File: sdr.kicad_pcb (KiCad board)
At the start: 4 copper layers, 65 x 56 mm, 224 parts, among them J1 RX, J2 TX, SW1 KMR231NGLFS, T1 B0322J5050, T2 B0322J5050, T3 TR_TC1-1-43X+, T4 TR_TC1-1-43X+, U1 FT601, U10 MIC94310, U11 PAM2305, U12 BGS12, U13 BGS12, U14 FT232HL, U15 93LCxxBT-I/OT, U3 LMS6002DR2, U4 ECP5, U5 Si5351, U6 PAM2305, U7 LD39200, U8 MIC94310, U9 MIC94310, X1 GSB443133HR, X2 JTAG, X3 RaspberryPiConnector, X4 JTAG, X5 USB_OTG, Y1 FL3000027, Y2 ABM11-141, Y3 ABLS2-12.000MHZ-D4Y-T

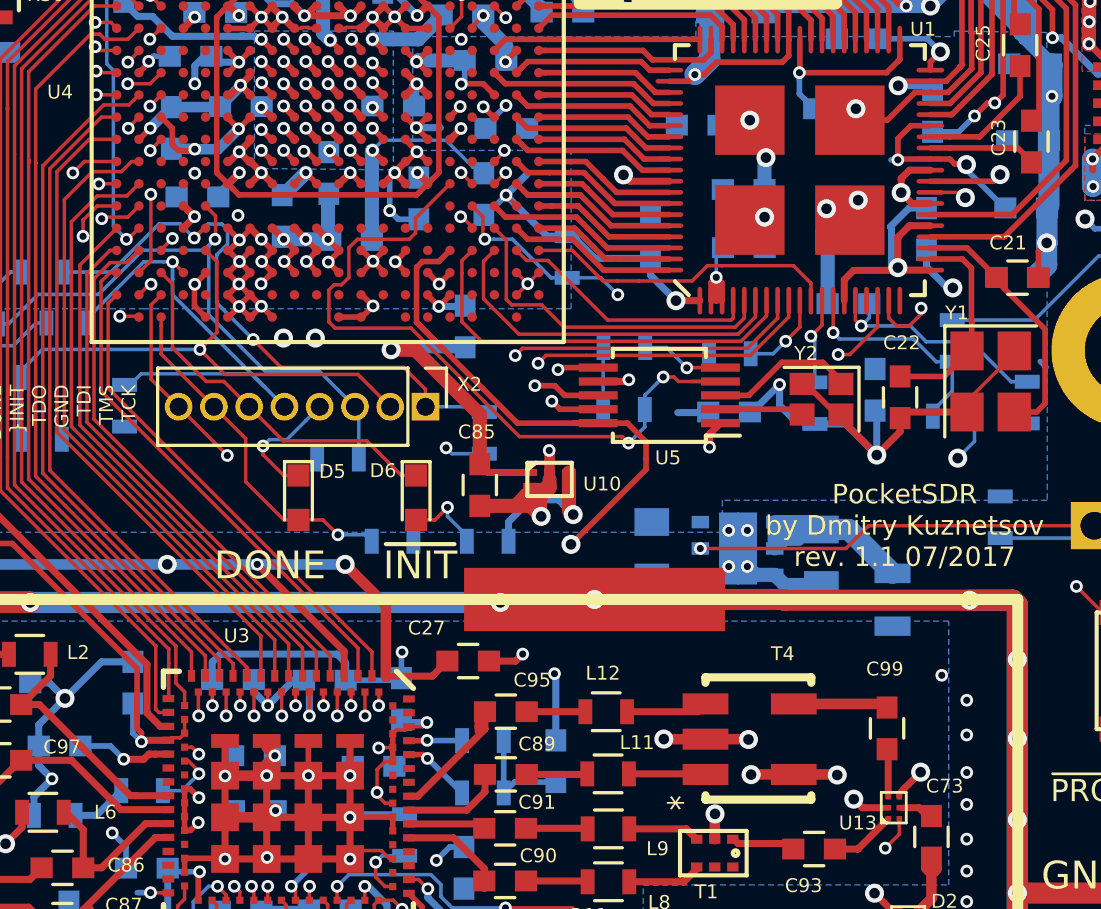
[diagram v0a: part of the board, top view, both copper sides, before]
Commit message: Update solder paste layer for components. Reduced width of tracks where they were wider than pads. Add mounting holes on paste layers.
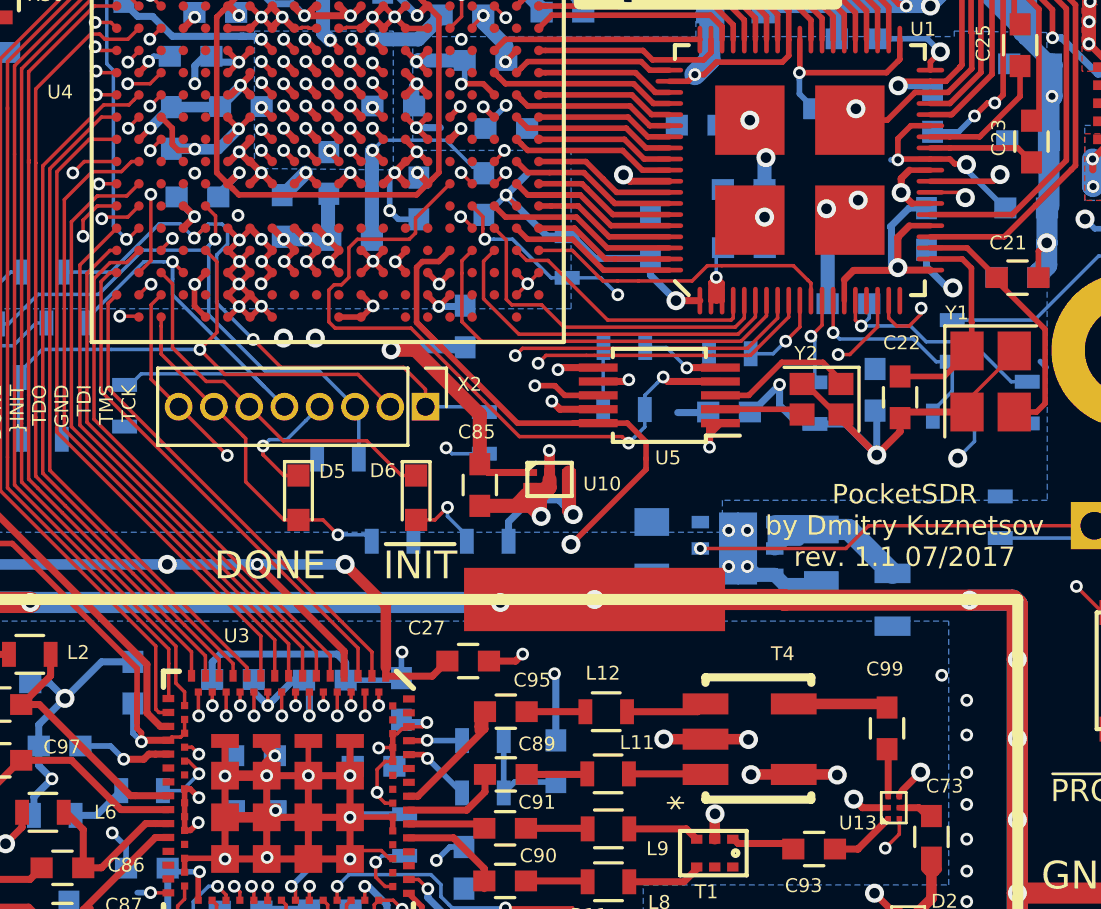
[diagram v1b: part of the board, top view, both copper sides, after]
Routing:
- net /FT601/I2C_SCL: track 26.7 -> 25.7 mm
- net VCCIO_FT: track 133.0 -> 133.7 mm

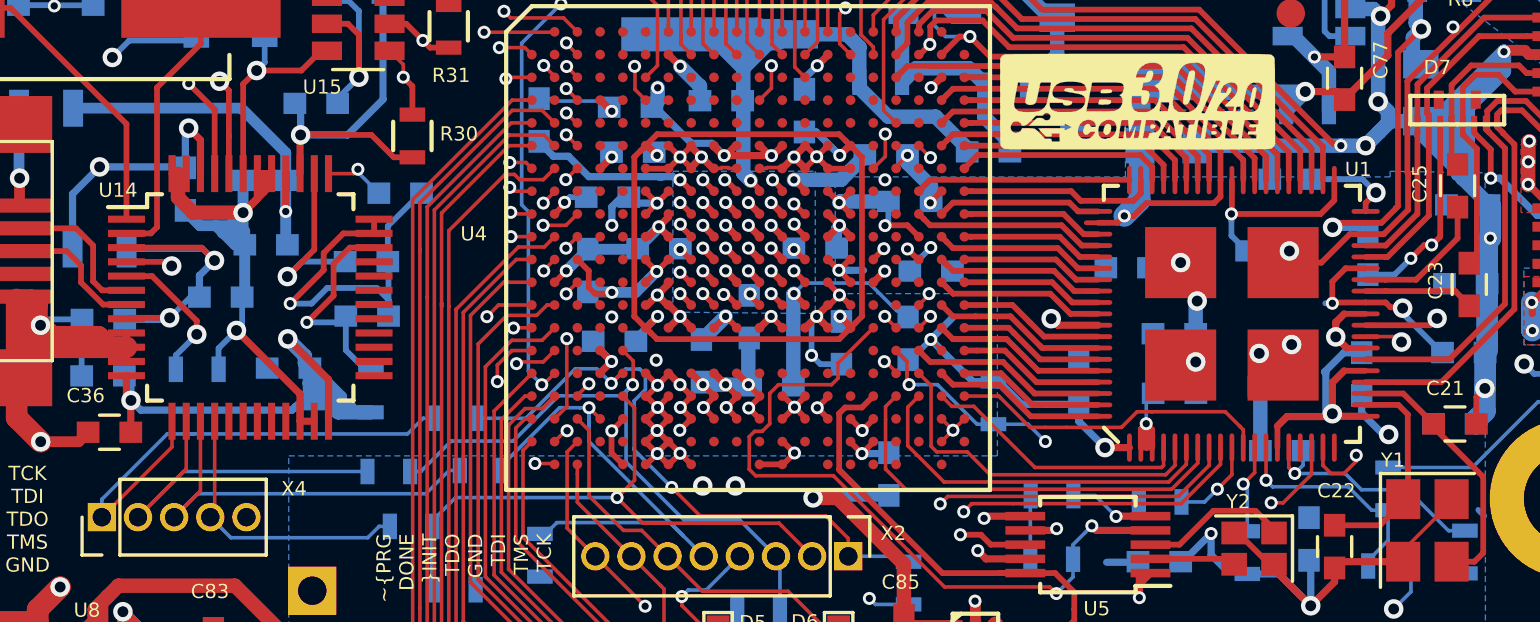
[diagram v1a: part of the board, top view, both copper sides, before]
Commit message: Update solder paste layers to reduce paste amount on some components and remove paste but not drill hole) on mount holes. Updated BOM. Removed deadend line on PCB. Add GND layer on Layer 3.
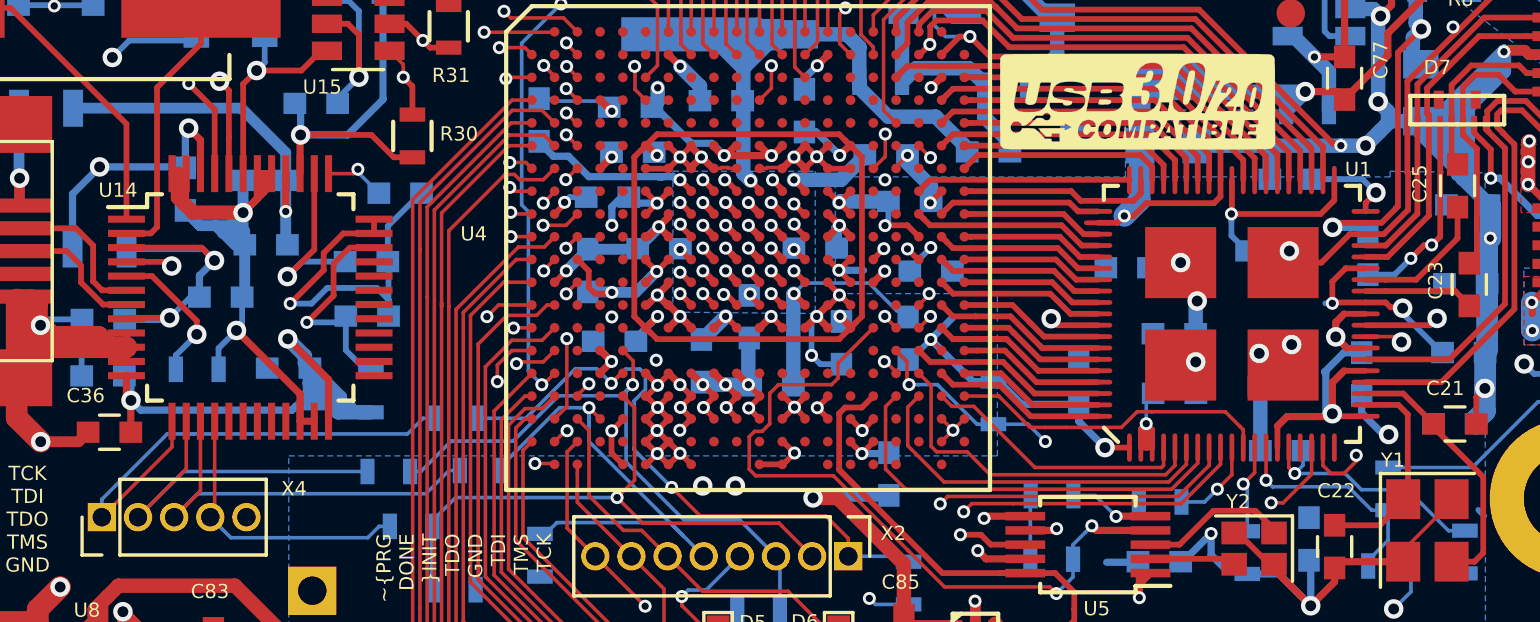
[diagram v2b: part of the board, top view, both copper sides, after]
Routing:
- net Net-(R39-Pad2): track 112.7 -> 49.4 mm
- net FT_GPIO1: track 72.3 -> 68.5 mm
- net GNDD: track 852.5 -> 853.6 mm
- added copper zone on In2.Cu, net GNDD

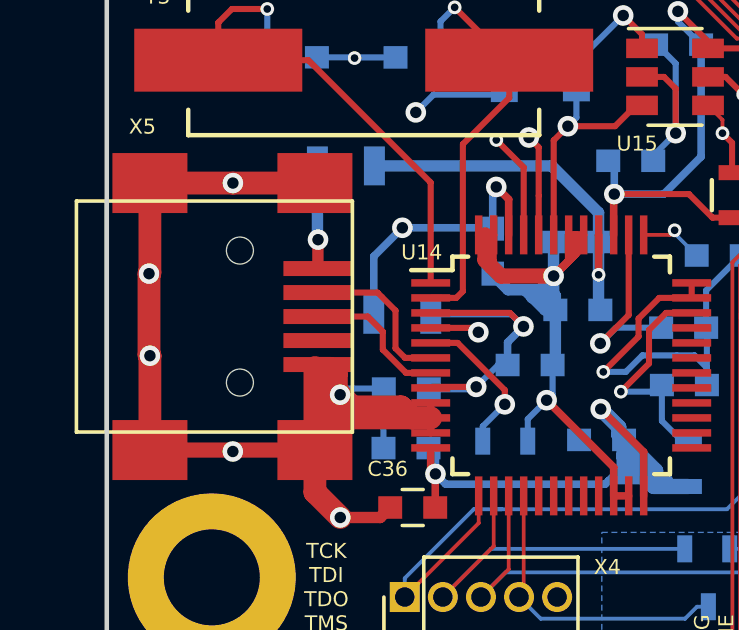
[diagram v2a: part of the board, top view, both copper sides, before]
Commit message: Fix USB mini B mount holes.
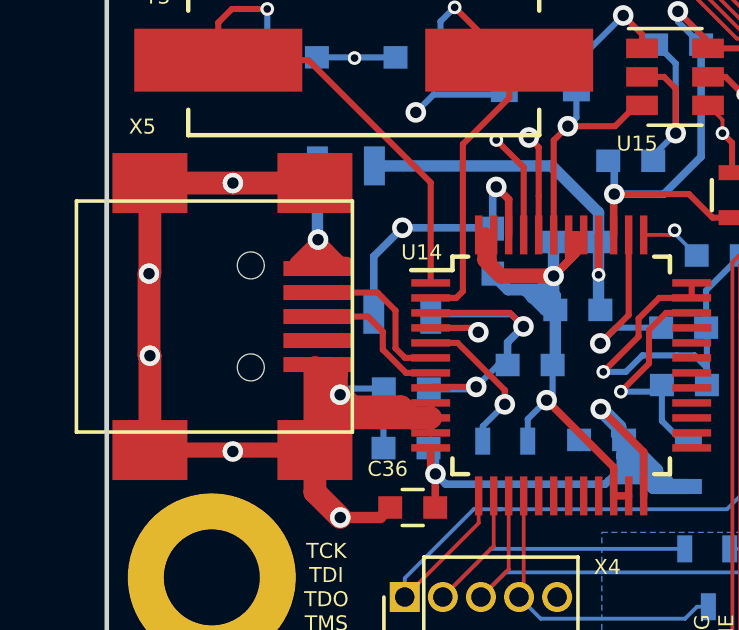
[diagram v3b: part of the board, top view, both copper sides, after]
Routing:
- net Net-(L13-Pad2): track 3.48 -> 7.55 mm
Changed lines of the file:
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@@
     (thickness 1.6)
     (drawings 27)
-    (tracks 3889)
+    (tracks 3897)
     (zones 0)
     (modules 224)
@@
     (0 F.Cu signal)
     (1 In1.Cu power hide)
-    (2 In2.Cu signal)
+    (2 In2.Cu signal hide)
     (31 B.Cu signal)
     (32 B.Adhes user hide)
@@
   )
   (setup
-    (last_trace_width 0.2032)
+    (last_trace_width 0.381)
     (user_trace_width 0.2032)
     (user_trace_width 0.254)
@@
     )
   )
-  (module Connectors:USB_Mini-B (layer F.Cu)
+  (module Connectors:USB_Mini-B locked (layer F.Cu)
     (at 104.23718 117.80556)
     (descr "USB Mini-B 5-pin SMD connector")
@@
     (pad 6 smd rect (at -2.8 4.45) (size 2.5 2) (layers F.Cu F.Paste F.Mask)
       (net 3 GNDD))
-    (pad "" np_thru_hole circle (at 0.2 -2.2) (size 0.9 0.9) (drill 0.9) (layers *.Cu *.Mask))
-    (pad "" np_thru_hole circle (at 0.2 2.2) (size 0.9 0.9) (drill 0.9) (layers *.Cu *.Mask))
+    (pad "" np_thru_hole circle (at 0.56282 -1.70556) (size 0.9 0.9) (drill 0.9) (layers *.Cu *.Mask))
+    (pad "" np_thru_hole circle (at 0.56282 1.69444) (size 0.9 0.9) (drill 0.9) (layers *.Cu *.Mask))
   )
   (module Inductors_SMD:L_0805 (layer B.Cu)
@@
   (segment (start 156.8577 133.25926) (end 159.80086 133.25926) (width 0.127) (layer B.Cu) (net 340))
   (segment (start 159.80086 133.25926) (end 160.24606 132.81406) (width 0.127) (layer B.Cu) (net 340))
+  (segment (start 106.875373 115.89258) (end 106.70286 115.89258) (width 0.381) (layer F.Cu) (net 341))
+  (segment (start 107.04068 115.24234) (end 107.04068 115.727273) (width 0.381) (layer F.Cu) (net 341))
+  (segment (start 107.04068 115.727273) (end 106.875373 115.89258) (width 0.381) (layer F.Cu) (net 341))
+  (segment (start 107.38612 115.58778) (end 107.38612 115.93576) (width 0.381) (layer F.Cu) (net 341))
+  (segment (start 107.04068 115.24234) (end 107.38612 115.58778) (width 0.381) (layer F.Cu) (net 341))
+  (segment (start 107.04068 115.24234) (end 106.28302 116) (width 0.381) (layer F.Cu) (net 341))
+  (segment (start 107.79834 116) (end 108 116) (width 0.381) (layer F.Cu) (net 341))
+  (segment (start 107.04068 115.24234) (end 107.79834 116) (width 0.381) (layer F.Cu) (net 341))
   (segment (start 107.02032 112.78362) (end 107.02032 115.22198) (width 0.381) (layer B.Cu) (net 341))
   (segment (start 107.02032 115.22198) (end 107.04068 115.24234) (width 0.381) (layer B.Cu) (net 341))

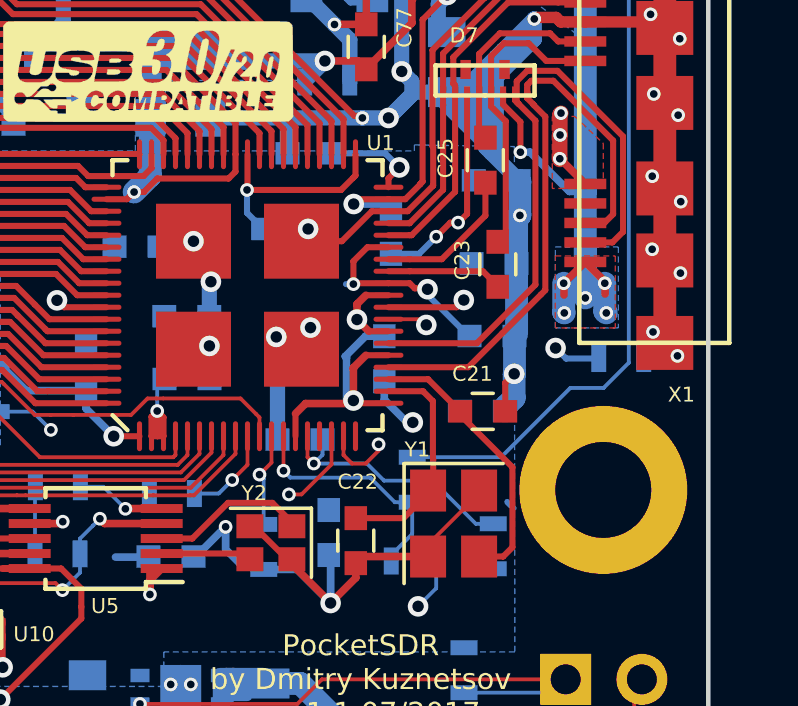
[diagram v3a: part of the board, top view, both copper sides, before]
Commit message: Small upgrade to make GND polygon on layer 3 more solid.
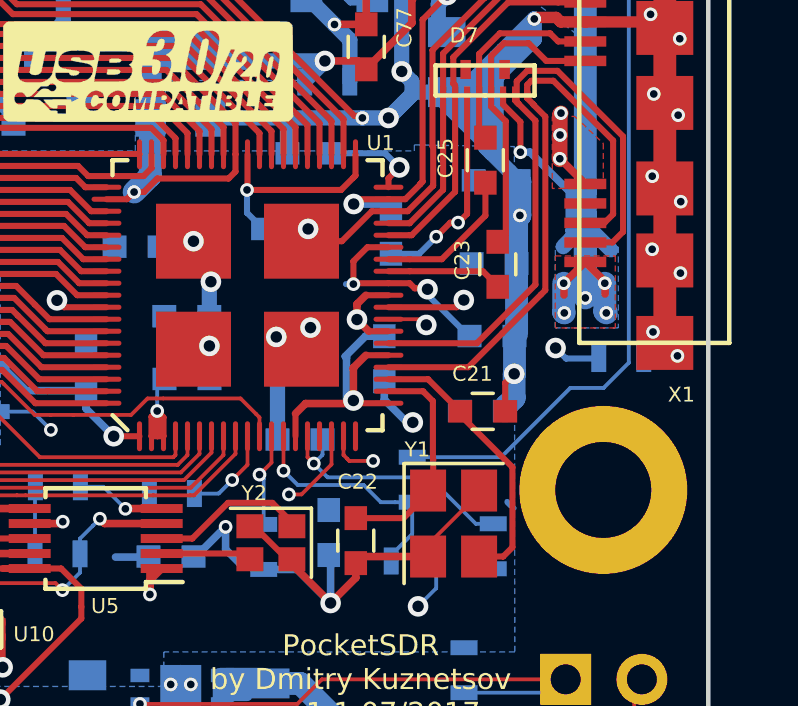
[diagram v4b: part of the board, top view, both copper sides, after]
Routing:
- net 5V_RPi: track 82.2 -> 87.7 mm
- net FT_GPIO1: track 68.5 -> 67.3 mm

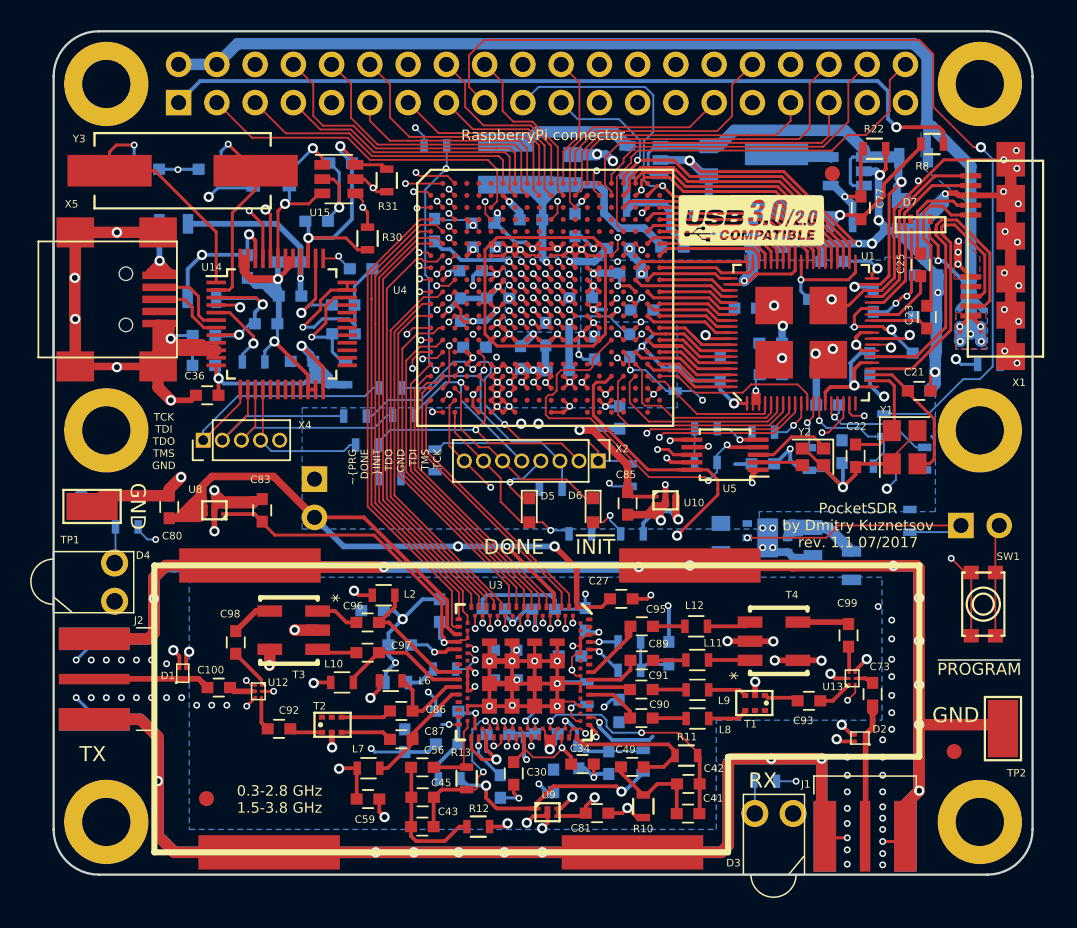
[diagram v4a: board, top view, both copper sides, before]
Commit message: Moved R1 to the same layer as FT600. Rotated Y1.
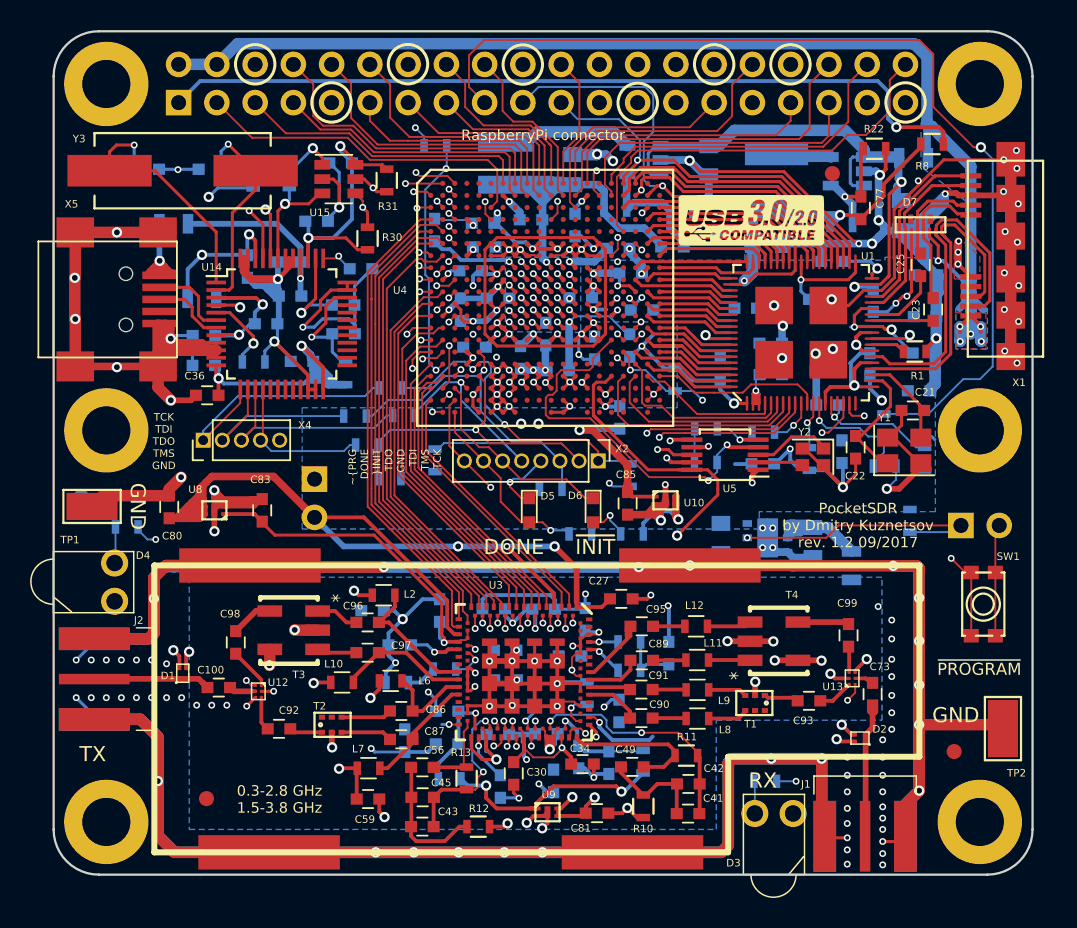
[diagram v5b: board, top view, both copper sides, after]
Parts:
- R1: moved to F.Cu
- moved R1 4.99 mm to (157.2, 121.3)
- moved C21 1.37 mm to (157.1, 125.2), turned to 180 degrees
- moved C23 0.66 mm to (158.4, 118.5)
- moved C22 0.57 mm to (153.3, 127.6)
- moved Y1 0.21 mm to (156.5, 127.8), turned to 0 degrees
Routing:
- net Net-(R1-Pad2): track 7.55 -> 2.28 mm, vias 2 -> 0
- net ~CFG_HOLD: track 73.3 -> 78.0 mm
- net /FT601/XO: track 9.33 -> 6.39 mm
- net ~RPI_OE: track 13.4 -> 16.3 mm
- net GNDD: track 853.6 -> 855.8 mm, vias 232 -> 231
- net /FT601/D-: track 22.3 -> 23.7 mm
- net /FT601/XI: track 7.52 -> 8.74 mm
- net /FT601/D+: track 20.6 -> 21.6 mm
- net /FT601/TX-: track 10.2 -> 9.51 mm
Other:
- board text added: "PocketSDR by Dmitry Kuznetsov rev. 1.2 09/2017"
- board text removed: "PocketSDR by Dmitry Kuznetsov rev. 1.1 07/2017"
